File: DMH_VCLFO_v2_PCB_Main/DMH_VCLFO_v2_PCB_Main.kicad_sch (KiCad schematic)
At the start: 0 parts

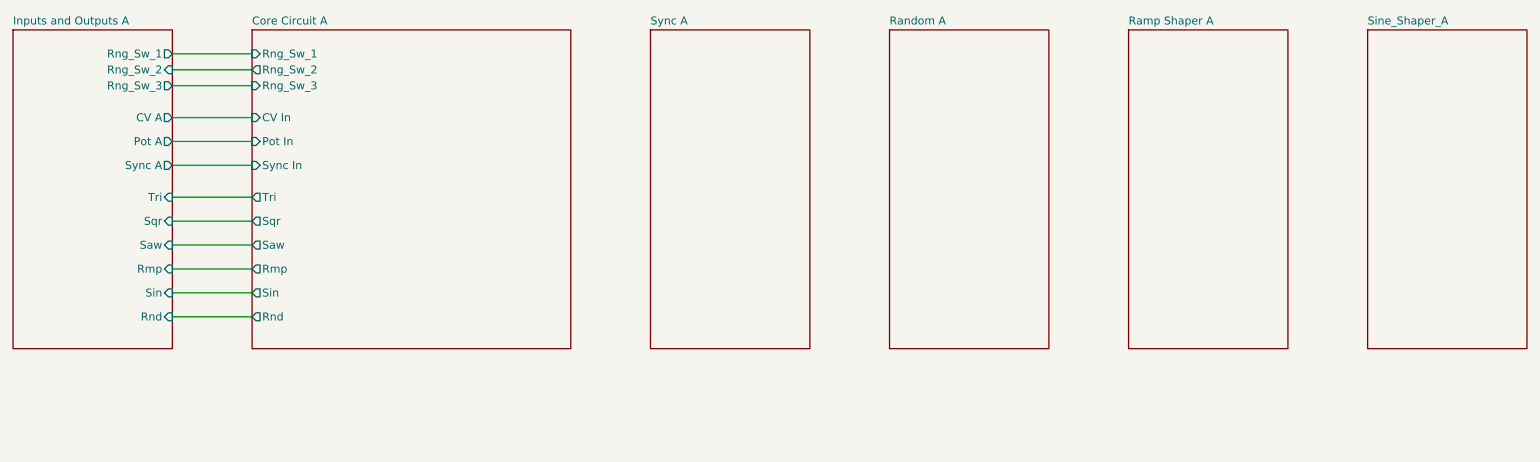
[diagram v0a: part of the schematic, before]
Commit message: Improved inter-PCB connections
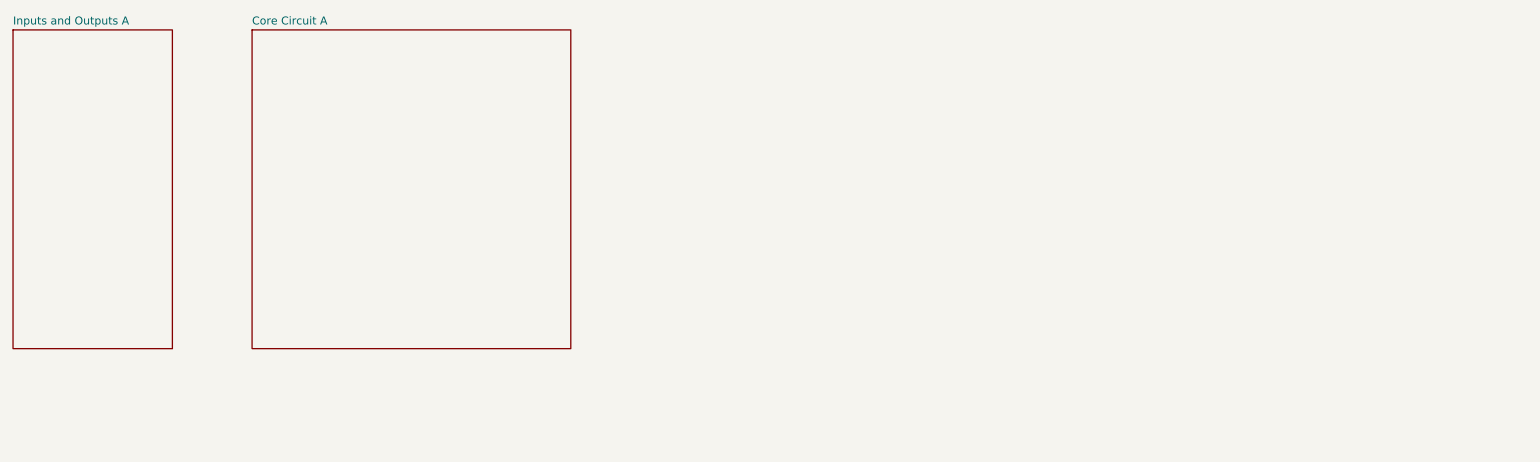
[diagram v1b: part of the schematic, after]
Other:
- removed sheet Ramp Shaper A
- removed sheet Random A
- removed sheet Sine_Shaper_A
- removed sheet Sync A
- sheet Core Circuit A ports: added none; removed CV In, Pot In, Rmp, Rnd, Rng_Sw_1, Rng_Sw_2, Rng_Sw_3, Saw, Sin, Sqr, Sync In, Tri
- sheet Inputs and Outputs A ports: added none; removed CV A, Pot A, Rmp, Rnd, Rng_Sw_1, Rng_Sw_2, Rng_Sw_3, Saw, Sin, Sqr, Sync A, Tri

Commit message: Notes from breadboarding
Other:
- added sheet Breadboard Layout v2 (Breadboard_Layout.kicad_sch)
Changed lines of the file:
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@@
+	)
+	(sheet
+		(at 76.2 165.1)
+		(size 38.1 25.4)
+		(exclude_from_sim no)
+		(in_bom yes)
+		(on_board yes)
+		(dnp no)
+		(fields_autoplaced yes)
+		(stroke
+			(width 0.1524)
+			(type solid)
+		)
+		(fill
+			(color 0 0 0 0.0000)
+		)
+		(property "Sheetname" "Breadboard Layout v2"
+			(at 76.2 164.3884 0)
+			(effects
+				(font
+					(size 1.27 1.27)
+				)
+				(justify left bottom)
+			)
+		)
+		(property "Sheetfile" "Breadboard_Layout.kicad_sch"
+			(at 76.2 191.0846 0)
+			(effects
+				(font
+					(size 1.27 1.27)
+				)
+				(justify left top)
+				(hide yes)
+			)
+		)
+		(instances
+			(project "DMH_VCLFO_v2_PCB_Main"
+				(path "/58f4306d-5387-4983-bb08-41a2313fd315"
+					(page "21")
+				)
+			)
+		)
 	)
 	(sheet

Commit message: Prepared for PCB design
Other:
- sheet Core Circuit A renamed SubModule A
- removed sheet Breadboard Layout
- added sheet Inputs and Outputs B (Inputs_and_Outputs_B.kicad_sch)
- added sheet Inputs and Outputs C (Inputs_and_Outputs_C.kicad_sch)
- added sheet SubModule B (Sub_module_B.kicad_sch)
- added sheet SubModule C (Sub_module_C.kicad_sch)
- sheet Inputs and Outputs A: file Inputs_and_Outputs.kicad_sch -> Inputs_and_Outputs_A.kicad_sch
- sheet SubModule A: file Core_Circuit.kicad_sch -> Sub_module_A.kicad_sch
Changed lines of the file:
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@@
 	(generator "eeschema")
 	(generator_version "9.0")
-	(paper "A4")
+	(paper "A4" portrait)
 	(title_block
 		(rev "1")
@@
 	)
 	(sheet
+		(at 63.5 152.4)
+		(size 50.8 50.8)
+		(exclude_from_sim no)
+		(in_bom yes)
+		(on_board yes)
+		(dnp no)
+		(fields_autoplaced yes)
+		(stroke
+			(width 0.1524)
+			(type solid)
+		)
+		(fill
+			(color 0 0 0 0.0000)
+		)
+		(property "Sheetname" "SubModule C"
+			(at 63.5 151.6884 0)
+			(effects
+				(font
+					(size 1.27 1.27)
+				)
+				(justify left bottom)
+			)
+		)
+		(property "Sheetfile" "Sub_module_C.kicad_sch"
+			(at 63.5 203.7846 0)
+			(effects
+				(font
+					(size 1.27 1.27)
+				)
+				(justify left top)
+				(hide yes)
+			)
+		)
+		(instances
+			(project "DMH_VCLFO_v2_PCB_Main"
+				(path "/58f4306d-5387-4983-bb08-41a2313fd315"
+					(page "7")
+				)
+			)
+		)
+	)
+	(sheet
 		(at 152.4 165.1)
-		(size 20.32 25.4)
+		(size 25.4 25.4)
 		(exclude_from_sim no)
 		(in_bom yes)
@@
 			(project "DMH_VCLFO_v2_PCB_Main"
 				(path "/58f4306d-5387-4983-bb08-41a2313fd315"
-					(page "10")
-				)
-			)
-		)
-	)
-	(sheet
-		(at 76.2 165.1)
+					(page "8")
+				)
+			)
+		)
+	)
+	(sheet
+		(at 25.4 152.4)
+		(size 25.4 50.8)
+		(exclude_from_sim no)
+		(in_bom yes)
+		(on_board yes)
+		(dnp no)
+		(fields_autoplaced yes)
+		(stroke
+			(width 0.1524)
+			(type solid)
+		)
+		(fill
+			(color 0 0 0 0.0000)
+		)
+		(property "Sheetname" "Inputs and Outputs C"
+			(at 25.4 151.6884 0)
+			(effects
+				(font
+					(size 1.27 1.27)
+				)
+				(justify left bottom)
+			)
+		)
+		(property "Sheetfile" "Inputs_and_Outputs_C.kicad_sch"
+			(at 25.4 203.7846 0)
+			(effects
+				(font
+					(size 1.27 1.27)
+				)
+				(justify left top)
+				(hide yes)
+			)
+		)
+		(instances
+			(project "DMH_VCLFO_v2_PCB_Main"
+				(path "/58f4306d-5387-4983-bb08-41a2313fd315"
+					(page "4")
+				)
+			)
+		)
+	)
+	(sheet
+		(at 63.5 88.9)
+		(size 50.8 50.8)
+		(exclude_from_sim no)
+		(in_bom yes)
+		(on_board yes)
+		(dnp no)
+		(fields_autoplaced yes)
+		(stroke
+			(width 0.1524)
+			(type solid)
+		)
+		(fill
+			(color 0 0 0 0.0000)
+		)
+		(property "Sheetname" "SubModule B"
+			(at 63.5 88.1884 0)
+			(effects
+				(font
+					(size 1.27 1.27)
+				)
+				(justify left bottom)
+			)
+		)
+		(property "Sheetfile" "Sub_module_B.kicad_sch"
+			(at 63.5 140.2846 0)
+			(effects
+				(font
+					(size 1.27 1.27)
+				)
+				(justify left top)
+				(hide yes)
+			)
+		)
+		(instances
+			(project "DMH_VCLFO_v2_PCB_Main"
+				(path "/58f4306d-5387-4983-bb08-41a2313fd315"
+					(page "6")
+				)
+			)
+		)
+	)
+	(sheet
+		(at 25.4 254)
 		(size 38.1 25.4)
 		(exclude_from_sim no)
@@
 		)
 		(property "Sheetname" "Breadboard Layout v2"
-			(at 76.2 164.3884 0)
+			(at 25.4 253.2884 0)
 			(effects
 				(font
@@
 		)
 		(property "Sheetfile" "Breadboard_Layout.kicad_sch"
-			(at 76.2 191.0846 0)
-			(effects
-				(font
-					(size 1.27 1.27)
-				)
-				(justify left top)
-				(hide yes)
-			)
-		)
-		(instances
-			(project "DMH_VCLFO_v2_PCB_Main"
-				(path "/58f4306d-5387-4983-bb08-41a2313fd315"
-					(page "21")
+			(at 25.4 279.9846 0)
+			(effects
+				(font
+					(size 1.27 1.27)
+				)
+				(justify left top)
+				(hide yes)
+			)
+		)
+		(instances
+			(project "DMH_VCLFO_v2_PCB_Main"
+				(path "/58f4306d-5387-4983-bb08-41a2313fd315"
+					(page "9")
 				)
 			)
@@
 			(color 0 0 0 0.0000)
 		)
-		(property "Sheetname" "Core Circuit A"
+		(property "Sheetname" "SubModule A"
 			(at 63.5 24.6884 0)
 			(effects
@@
 			)
 		)
-		(property "Sheetfile" "Core_Circuit.kicad_sch"
+		(property "Sheetfile" "Sub_module_A.kicad_sch"
 			(at 63.5 76.7846 0)
 			(effects
@@
 			(project "DMH_VCLFO_v2_PCB_Main"
 				(path "/58f4306d-5387-4983-bb08-41a2313fd315"
+					(page "5")
+				)
+			)
+		)
+	)
+	(sheet
+		(at 25.4 88.9)
+		(size 25.4 50.8)
+		(exclude_from_sim no)
+		(in_bom yes)
+		(on_board yes)
+		(dnp no)
+		(fields_autoplaced yes)
+		(stroke
+			(width 0.1524)
+			(type solid)
+		)
+		(fill
+			(color 0 0 0 0.0000)
+		)
+		(property "Sheetname" "Inputs and Outputs B"
+			(at 25.4 88.1884 0)
+			(effects
+				(font
+					(size 1.27 1.27)
+				)
+				(justify left bottom)
+			)
+		)
+		(property "Sheetfile" "Inputs_and_Outputs_B.kicad_sch"
+			(at 25.4 140.2846 0)
+			(effects
+				(font
+					(size 1.27 1.27)
+				)
+				(justify left top)
+				(hide yes)
+			)
+		)
+		(instances
+			(project "DMH_VCLFO_v2_PCB_Main"
+				(path "/58f4306d-5387-4983-bb08-41a2313fd315"
 					(page "3")
-				)
-			)
-		)
-	)
-	(sheet
-		(at 25.4 165.1)
-		(size 38.1 25.4)
-		(exclude_from_sim no)
-		(in_bom yes)
-		(on_board yes)
-		(dnp no)
-		(fields_autoplaced yes)
-		(stroke
-			(width 0.1524)
-			(type solid)
-		)
-		(fill
-			(color 0 0 0 0.0000)
-		)
-		(property "Sheetname" "Breadboard Layout"
-			(at 25.4 164.3884 0)
-			(effects
-				(font
-					(size 1.27 1.27)
-				)
-				(justify left bottom)
-			)
-		)
-		(property "Sheetfile" "Breadboard_Layout.kicad_sch"
-			(at 25.4 191.0846 0)
-			(effects
-				(font
-					(size 1.27 1.27)
-				)
-				(justify left top)
-				(hide yes)
-			)
-		)
-		(instances
-			(project "DMH_VCLFO_v2_PCB_Main"
-				(path "/58f4306d-5387-4983-bb08-41a2313fd315"
-					(page "20")
 				)
 			)
@@
 			)
 		)
-		(property "Sheetfile" "Inputs_and_Outputs.kicad_sch"
+		(property "Sheetfile" "Inputs_and_Outputs_A.kicad_sch"
 			(at 25.4 76.7846 0)
 			(effects

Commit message: Added project with Single VCLFO schematic
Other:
- removed sheet Breadboard Layout v2
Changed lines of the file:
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@@
-	)
-	(sheet
-		(at 25.4 254)
-		(size 38.1 25.4)
-		(exclude_from_sim no)
-		(in_bom yes)
-		(on_board yes)
-		(dnp no)
-		(fields_autoplaced yes)
-		(stroke
-			(width 0.1524)
-			(type solid)
-		)
-		(fill
-			(color 0 0 0 0.0000)
-		)
-		(property "Sheetname" "Breadboard Layout v2"
-			(at 25.4 253.2884 0)
-			(effects
-				(font
-					(size 1.27 1.27)
-				)
-				(justify left bottom)
-			)
-		)
-		(property "Sheetfile" "Breadboard_Layout.kicad_sch"
-			(at 25.4 279.9846 0)
-			(effects
-				(font
-					(size 1.27 1.27)
-				)
-				(justify left top)
-				(hide yes)
-			)
-		)
-		(instances
-			(project "DMH_VCLFO_v2_PCB_Main"
-				(path "/58f4306d-5387-4983-bb08-41a2313fd315"
-					(page "9")
-				)
-			)
-		)
 	)
 	(sheet
